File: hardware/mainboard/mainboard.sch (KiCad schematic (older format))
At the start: 3 parts, among them J4 left header, J5 right header

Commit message: Create hardware revision mainboard v3
This addresses an issue with the ramp oscillators using the wrong type of transistor.
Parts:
- J4, J5: dnp (none) -> 1
- MH1: dnp (none) -> 1; finalized (none) -> yes
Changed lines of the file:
@@
 Sheet 1 7
 Title "Castor & Pollux"
-Date "2020-09-26"
-Rev "v2"
+Date "2021-01-27"
+Rev "v3"
 Comp "Winterbloom"
 Comment1 "CERN-OHL-P v2"
@@
 F 5 "4UCON 21790" H 2400 6750 50  0001 C CNN "mpn"
 F 6 "" H 2400 6750 50  0001 C CNN "mpn alt"
+F 7 "1" H 2400 6750 50  0001 C CNN "dnp"
 	1    2400 6750
 	1    0    0    1
@@
 F 5 "4UCON 21790" H 3100 6750 50  0001 C CNN "mpn"
 F 6 "" H 3100 6750 50  0001 C CNN "mpn alt"
+F 7 "1" H 3100 6750 50  0001 C CNN "dnp"
 	1    3100 6750
 	-1   0    0    1
@@
 F 2 "MountingHole:MountingHole_3.2mm_M3_Pad_Via" H 6350 6200 50  0001 C CNN
 F 3 "~" H 6350 6200 50  0001 C CNN
+F 4 "1" H 6350 6200 50  0001 C CNN "dnp"
+F 5 "yes" H 6350 6200 50  0001 C CNN "finalized"
 	1    6350 6200
 	1    0    0    -1

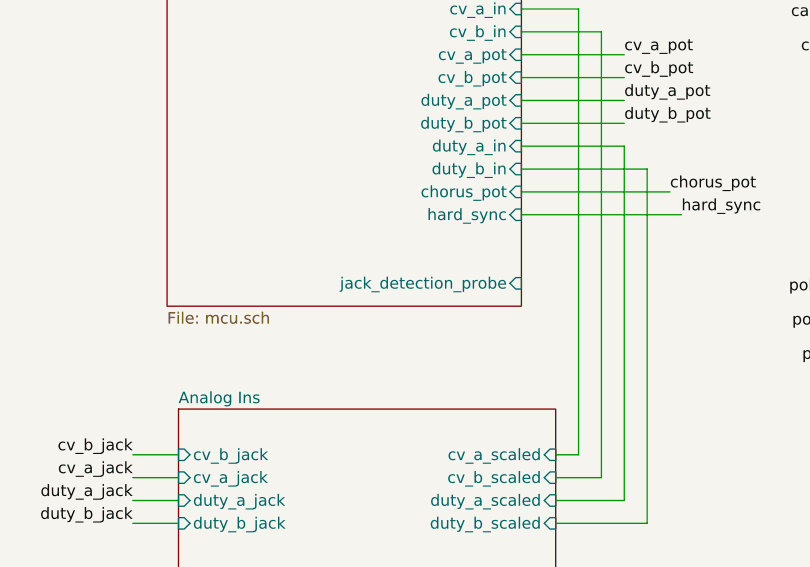
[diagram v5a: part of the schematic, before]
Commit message: hardware: finish up mpn assignments for mainboard
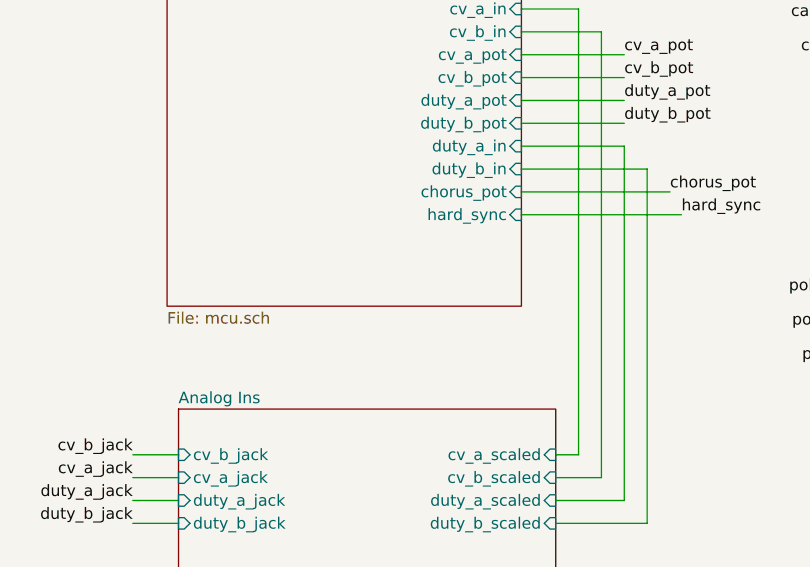
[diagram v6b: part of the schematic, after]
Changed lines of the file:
@@
 F16 "duty_a_in" I R 2800 2550 50
 F17 "duty_b_in" I R 2800 2650 50
-F18 "jack_detection_probe" I R 2800 3150 50
-F19 "hard_sync" I R 2800 2850 50
-F20 "chorus_pot" I R 2800 2750 50
+F18 "hard_sync" I R 2800 2850 50
+F19 "chorus_pot" I R 2800 2750 50
 $EndSheet
 $Sheet
